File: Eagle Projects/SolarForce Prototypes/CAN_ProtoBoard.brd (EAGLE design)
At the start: 100 x 80 mm, 18 parts, among them U1 MCP2551

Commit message: CAN ProtoPCB V1 Ready..
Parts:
- removed JP1: (no value), SparkFun-Connectors:DB9_MALE
- added !INT, CLKOUT, RX, RX0BF, RX1BF, TX, TX0RTS, TX1RTS, TX2RTS, VBAT, VREF: (no value), pinhead:1X01
- added C11: 100uF, resistor:PANASONIC_D
- added C5, C6: 560pF, resistor:C0805K
- added CAN: (no value), pinhead:1X04
- added CANSCREW: (no value), con-wago-500:W237-103
- added DB9M: (no value), SparkFun-Connectors:DB9_MALE
- added IO: (no value), pinhead:1X10
- added JLINE, KLINE: (no value), pinhead:1X03
- added R7: 120E, resistor:R0805
- added R8, R9: 100E, resistor:R0805
- added SJ1: Term, SparkFun-Retired:SJ_2S-TRACE
- Q1: value (none) -> 16MHz
- R3, R4, R6: value (none) -> 1k
- moved LED3 63.9 mm to (27.8, 26.4), turned to 180 degrees
- moved U1 62.7 mm to (36.8, 24.1)
- moved C3 61.0 mm to (36.8, 17.3), turned to 180 degrees
- moved C4 57.3 mm to (26.0, 9.53), turned to 270 degrees
- moved R3 57.1 mm to (24.8, 31.0), turned to 90 degrees
- moved LED2 54.8 mm to (24.8, 26.5), turned to 180 degrees
- moved Q1 54.0 mm to (17.8, 24.1), turned to 180 degrees
- moved R1 53.4 mm to (31.8, 24.1), turned to 270 degrees
- moved C1 51.9 mm to (15.4, 29.2), turned to 270 degrees
- moved R4 43.2 mm to (27.8, 31.0), turned to 90 degrees
- moved R5 42.6 mm to (26.0, 13.5), turned to 270 degrees
- moved U$1 38.2 mm to (20.3, 15.2), turned to 270 degrees
- moved C2 37.1 mm to (20.2, 29.2), turned to 270 degrees
- moved R2 36.1 mm to (6.10, 7.75), turned to 270 degrees
- moved R6 35.2 mm to (8.51, 7.75), turned to 270 degrees
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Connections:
- new net CLKOUT: CLKOUT.1, U$1.3
- new net N$10: U1.5, VREF.1
- new net N$11: C5.2, R8.1
- new net N$12: C6.2, R9.1
- new net N$16: IO.3
- new net N$9: R7.1, SJ1.2
- new net RX0BF: RX0BF.1, U$1.12
- new net RX1BF: RX1BF.1, U$1.11
- new net TX0RTS: TX0RTS.1, U$1.4
- new net TX1RTS: TX1RTS.1, U$1.5
- new net TX2RTS: TX2RTS.1, U$1.7
- net +5V: now also C11.+, CAN.4, IO.10, IO.2
- net CANH: now also CAN.3, CANSCREW.1, DB9M.3, R9.2, SJ1.1; no longer JP1.3
- net CANL: now also CAN.2, CANSCREW.2, DB9M.5, R7.2, R8.2; no longer JP1.5
- net CS: now also IO.8
- net GND: now also C11.-, C5.1, C6.1, CAN.1, CANSCREW.3, DB9M.2, IO.1, IO.9, JLINE.1, KLINE.1; no longer JP1.2
- net INT: now also !INT.1, IO.4
- net J+: now also DB9M.7, JLINE.3; no longer JP1.7
- net J-: now also DB9M.6, JLINE.2; no longer JP1.6
- net K: now also DB9M.4, KLINE.3; no longer JP1.4
- net L: now also DB9M.8, KLINE.2; no longer JP1.8
- net RXCAN: now also RX.1
- net SCK: now also IO.5
- net SI: now also IO.6
- net SO: now also IO.7
- net TXCAN: now also TX.1
- net VBAT: now also DB9M.9, VBAT.1; no longer JP1.9
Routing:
- net +5V: track 0.00 -> 122.4 mm
- net CANL: track 0.00 -> 67.4 mm
- net CANH: track 0.00 -> 55.2 mm
- net GND: track 0.00 -> 44.7 mm, vias 0 -> 5
- net RXCAN: track 0.00 -> 38.3 mm
- net J-: track 0.00 -> 31.0 mm
- net J+: track 0.00 -> 27.5 mm
- net INT: track 0.00 -> 23.7 mm
- net TXCAN: track 0.00 -> 23.0 mm
- net L: track 0.00 -> 19.1 mm
- net K: track 0.00 -> 13.1 mm
- net TX0RTS: track 0.00 -> 12.0 mm
- net VBAT: track 0.00 -> 12.0 mm
- net TX1RTS: track 0.00 -> 11.6 mm
- net N$1: track 0.00 -> 11.0 mm
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- added copper zone on layer 16, net GND
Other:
- board size 100 x 80 mm -> 50 x 50 mm
- board text added: "5V"
- board text added: "CAN BUS"
- board text added: "CANH"
- board text added: "CANL"
- board text added: "CS"
- board text added: "DIYElectronics.co.za"
- board text added: "Demo Board"
- board text added: "GND"
- board text added: "INT"
- board text added: "J+"
- board text added: "J-"
- board text added: "K"
- board text added: "L"
- board text added: "R Mawbey | UKZN | 2015"
- board text added: "SCK"
- board text added: "SI"
- board text added: "SO"
- board text added: "rambo@rambo.co.za"

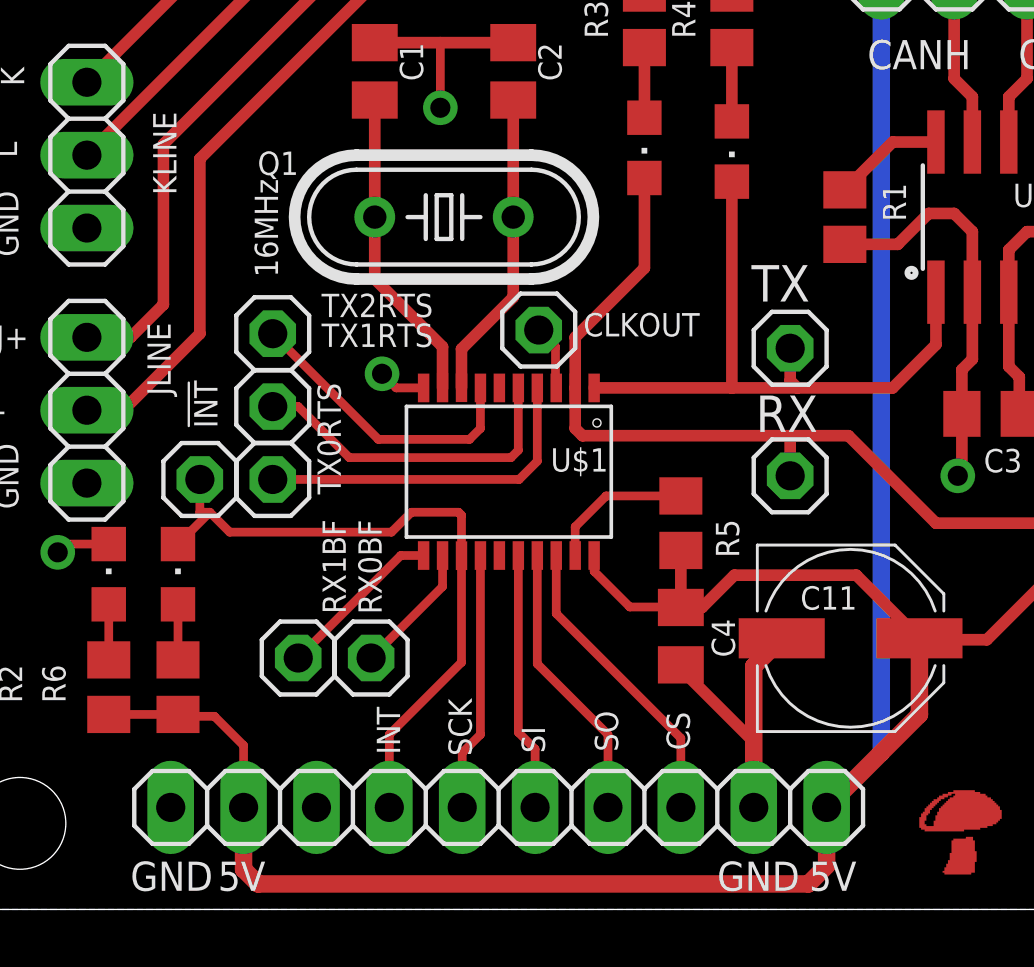
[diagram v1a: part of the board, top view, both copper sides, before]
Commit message: Used wrong package for MCP2515.. SO not TSSOP!! Changed and fixxed...
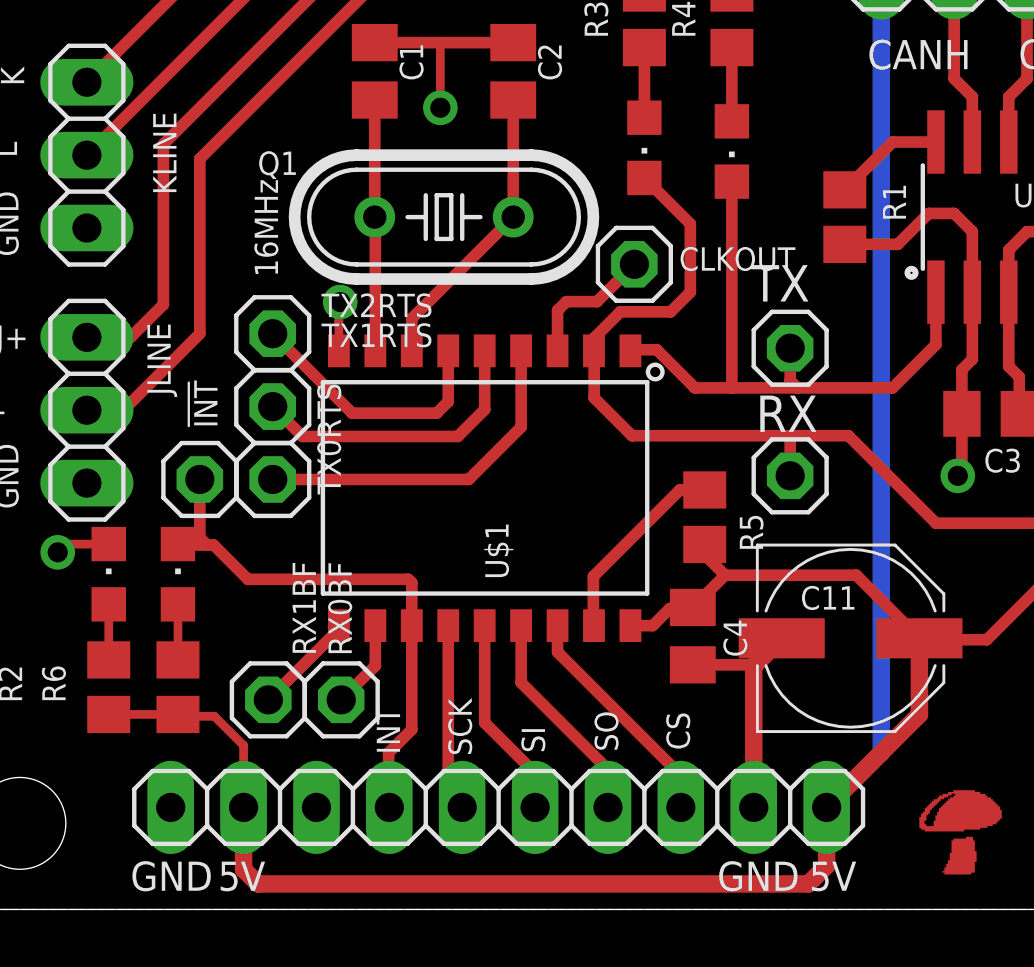
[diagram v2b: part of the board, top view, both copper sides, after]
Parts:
- U$1: device RobThePyro:TSSOP20 -> RobThePyro:SO-18W
- moved CLKOUT 4.05 mm to (24.4, 22.5)
- moved RX1BF 1.79 mm to (11.7, 7.30)
- moved RX0BF 1.79 mm to (14.2, 7.30)
- moved U$1 1.25 mm to (19.2, 14.7), turned to 180 degrees
- moved R5 0.86 mm to (26.9, 13.7)
- moved C4 0.42 mm to (26.5, 9.53)
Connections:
- net +5V: now also U$1.18; no longer U$1.20
- net CS: now also U$1.16; no longer U$1.18
- net GND: now also U$1.9; no longer U$1.10
- net INT: now also U$1.12; no longer U$1.13
- net N$1: now also U$1.8; no longer U$1.9
- net N$2: now also U$1.7; no longer U$1.8
- net N$5: now also U$1.17; no longer U$1.19
- net RX0BF: now also U$1.11; no longer U$1.12
- net RX1BF: now also U$1.10; no longer U$1.11
- net SCK: now also U$1.13; no longer U$1.14
- net SI: now also U$1.14; no longer U$1.16
- net SO: now also U$1.15; no longer U$1.17
- net TX2RTS: now also U$1.6; no longer U$1.7
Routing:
- net INT: track 23.7 -> 19.3 mm
- net +5V: track 122.4 -> 119.7 mm
- net SCK: track 9.04 -> 6.54 mm
- net CLKOUT: track 2.27 -> 4.75 mm
- net CS: track 10.6 -> 8.14 mm
- net N$1: track 11.0 -> 8.75 mm
- net RX1BF: track 5.85 -> 3.61 mm
- net SO: track 9.80 -> 7.59 mm
- net SI: track 9.02 -> 7.08 mm
- net N$5: track 5.13 -> 6.85 mm
- net RX0BF: track 4.60 -> 3.08 mm
- net TX1RTS: track 11.6 -> 10.3 mm
- net TX2RTS: track 10.3 -> 9.20 mm
- net GND: track 44.7 -> 43.6 mm
- net RXCAN: track 38.3 -> 39.1 mm
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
